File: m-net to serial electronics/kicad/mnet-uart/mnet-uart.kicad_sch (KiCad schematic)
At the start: 11 parts, among them U1 LM741, U2 LM741

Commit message: kicad schematics draft1
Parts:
- added C3: 1uF, symbol Device:C
- added C4: 100nF, symbol Device:C
- added J2: Screw_Terminal_01x02, symbol Connector:Screw_Terminal_01x02
- added Q?: 2N7002K, Package_TO_SOT_SMD:SOT-23, symbol Transistor_FET:2N7002K
- added R?: 1.8k, symbol Device:R
- added R? (x2): 10k, symbol Device:R
- added R?: 1k, symbol Device:R
- added U3: 74LS04, symbol 74xx:74LS04
- added U4: NA555P, Package_DIP:DIP-8_W7.62mm, symbol Timer:NA555P
- gave numbers to parts that had none: 1
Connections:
- net +5V: now also R?.1, R?.1, R?.1, U4.4 (R), U4.8 (VCC)
- net GND: now also C4.1, J2.2 (Pin_2), U4.1 (GND)
- net at U2.6: now also U3.1
- new net: C3.1, U3.2
- new net: C3.2, R?.2, U4.2 (TR)
- new net: C4.2, R?.2, U4.6 (THR), U4.7 (DIS)
- new net: Q?.2 (S), R?.2, U4.3 (Q)
- new net: Q?.3 (D), R?.2
- new net +3.3V: J2.1 (Pin_1), Q?.1 (G), R?.1
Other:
- moved on the sheet: C1, C2, J1, R1, R2, R3, R4, R?, U1, U2

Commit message: comments
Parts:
- gave numbers to parts that had none: 7
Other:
- moved on the sheet: R10

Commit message: Schematics and layout updates
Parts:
- C1, C2, C3, C4: footprint (none) -> Capacitor_SMD:C_0805_2012Metric
- J1, J2: footprint (none) -> TerminalBlock_Phoenix:TerminalBlock_Phoenix_MKDS-1,5-2-5.08_1x02_P5.08mm_Horizontal
- R1, R10, R2, R3, R4, R5, R6, R7, R8, R9: footprint (none) -> Resistor_SMD:R_0805_2012Metric
- U1, U2: footprint (none) -> Package_DIP:DIP-8_W7.62mm
- U3: footprint (none) -> Package_DIP:DIP-14_W7.62mm
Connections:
- net +3.3V: no longer J2.1 (Pin_1)
- net at Q1.3 (D), R10.2: now also J2.1 (Pin_1)

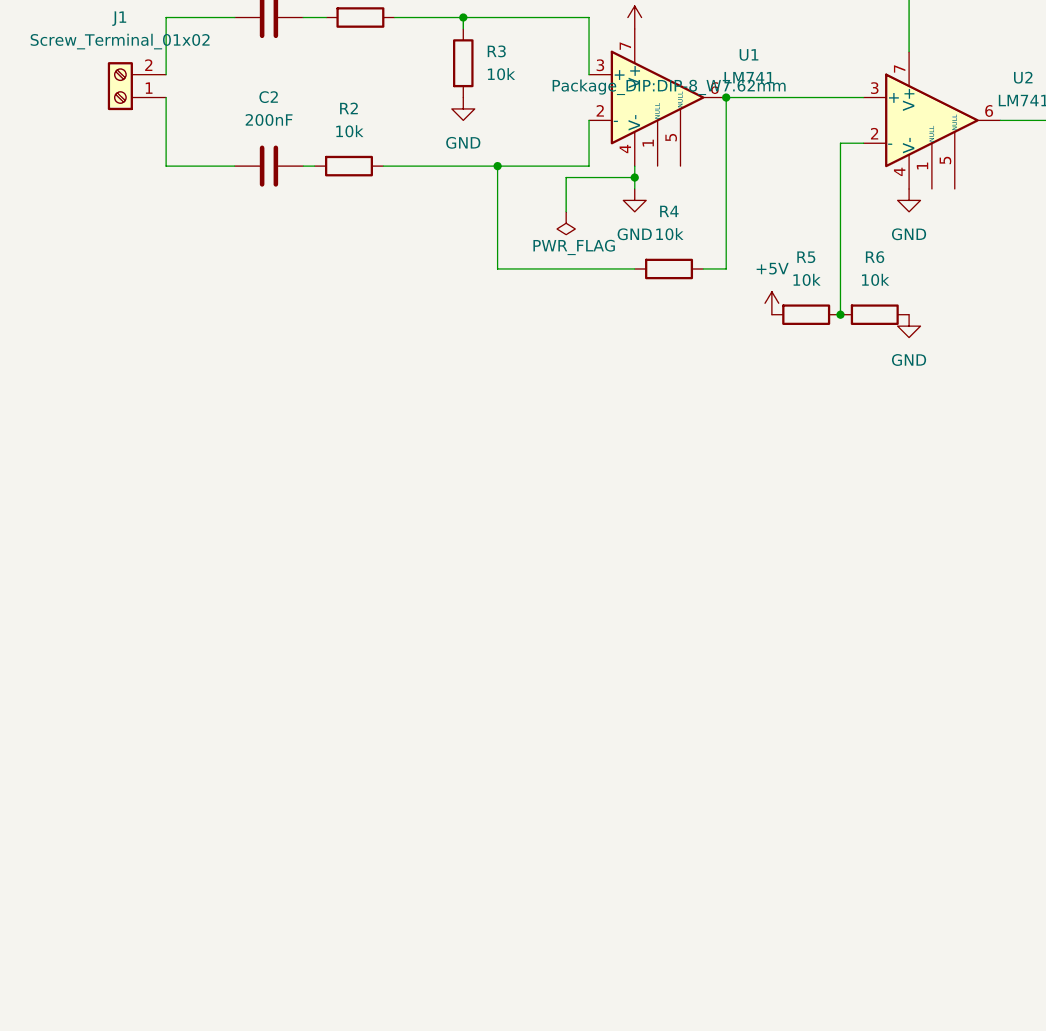
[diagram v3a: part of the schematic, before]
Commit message: added power supply
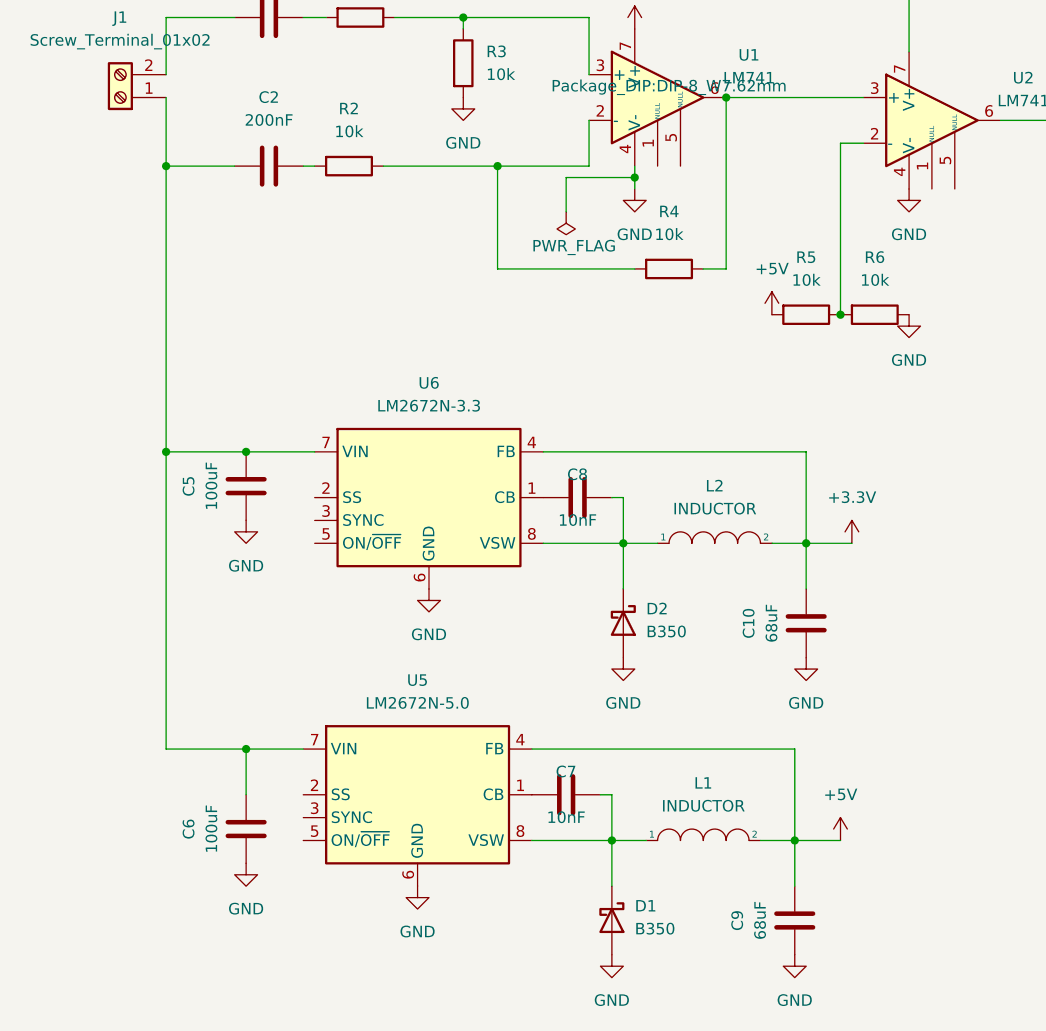
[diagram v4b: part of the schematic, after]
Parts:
- added C10, C9: 68uF, Capacitor_SMD:C_0805_2012Metric, symbol Device:C
- added C5, C6: 100uF, Capacitor_SMD:C_0805_2012Metric, symbol Device:C
- added C7, C8: 10nF, Capacitor_SMD:C_0805_2012Metric, symbol Device:C
- added D1, D2: B350, Diode_SMD:D_SMC, symbol Diode:B350
- added L1, L2: INDUCTOR, Inductor_THT:L_Axial_L6.6mm_D2.7mm_P10.16mm_Horizontal_Vishay_IM-2, symbol pspice:INDUCTOR
- added U5: LM2672N-5.0, Package_DIP:DIP-8_W7.62mm, symbol Regulator_Switching:LM2672N-5.0
- added U6: LM2672N-3.3, Package_DIP:DIP-8_W7.62mm, symbol Regulator_Switching:LM2672N-3.3
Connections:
- net +3.3V: now also C10.1, L2.2, U6.4 (FB)
- net +5V: now also C9.1, L1.2, U5.4 (FB)
- net GND: now also C10.2, C5.2, C6.2, C9.2, D1.2 (A), D2.2 (A), U5.6 (GND), U6.6 (GND)
- net at C2.2, J1.1 (Pin_1): now also C5.1, C6.1, U5.7 (VIN), U6.7 (VIN)
- new net: C8.2, D2.1 (K), L2.1, U6.8 (VSW)
- new net: C8.1, U6.1 (CB)
- new net: C7.1, U5.1 (CB)
- new net: C7.2, D1.1 (K), L1.1, U5.8 (VSW)
